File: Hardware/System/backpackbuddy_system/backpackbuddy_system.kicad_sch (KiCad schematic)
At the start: 1 part

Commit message: more changes
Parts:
- removed U?: ATmega32U4-A, Package_QFP:TQFP-44_10x10mm_P0.8mm, symbol MCU_Microchip_ATmega:ATmega32U4-A
- added J?: Ultrasonic 1, symbol Connector_Generic:Conn_01x04
- added J?: PIR, symbol Connector_Generic:Conn_01x03
- added J?: Ultrasonic 2, symbol Connector_Generic:Conn_01x04
- added J?: ESP8266, symbol Connector_Generic:Conn_01x08
- added SW?: RESET, symbol Switch:SW_Push
- added U?: ATmega32U4-A, Package_QFP:TQFP-44_10x10mm_P0.8mm, symbol MCU_Microchip_ATmega:ATmega32U4-A
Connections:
- net microcontroller/PB0: now also J?.3 (Pin_3)
- net microcontroller/PB1: now also J?.5 (Pin_5)
- net microcontroller/PB2: now also J?.2 (Pin_2)
- net microcontroller/PD0: now also J?.3 (Pin_3)
- net microcontroller/PD1: now also J?.2 (Pin_2)
- net microcontroller/PD4: now also J?.3 (Pin_3)
- net microcontroller/PD5: now also J?.2 (Pin_2)
- new net: J?.6 (Pin_6), SW?.1
- new net: U?.14 (VCC), U?.34 (VCC)
- new net: U?.15 (GND), U?.23 (GND), U?.35 (GND), U?.43 (GND)
- new net: U?.24 (AVCC), U?.44 (AVCC)
- new net +3V3: J?.4 (Pin_4), J?.8 (Pin_8)
- new net +5V: J?.3 (Pin_3), J?.4 (Pin_4), J?.4 (Pin_4)
- new net GND: J?.1 (Pin_1), J?.1 (Pin_1), J?.1 (Pin_1), J?.1 (Pin_1), SW?.2
- new net microcontroller/PD2/RX: J?.7 (Pin_7)
- new net microcontroller/PD3/TX: J?.2 (Pin_2)
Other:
- sheet microcontroller ports: added PD2/RX, PD3/TX; removed PB3, PB4, PB5, PB6, PB7, PC6, PC7, PD2, PD3

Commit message: vibration stuff
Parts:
- removed U?: ATmega32U4-A, Package_QFP:TQFP-44_10x10mm_P0.8mm, symbol MCU_Microchip_ATmega:ATmega32U4-A
- added J?: Left Vibration 2, symbol Connector_Generic:Conn_01x03
- added J?: Left Vibration 1, symbol Connector_Generic:Conn_01x03
- added J?: Right Vibration 2, symbol Connector_Generic:Conn_01x03
- added J?: Right Vibration 1, symbol Connector_Generic:Conn_01x03
- added Q? (x2): Q_NMOS_GDS, symbol Device:Q_NMOS_GDS
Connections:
- net +3V3: now also Q?.2 (D), Q?.2 (D)
- net GND: now also J?.1 (Pin_1), J?.1 (Pin_1), J?.1 (Pin_1), J?.1 (Pin_1), J?.3 (Pin_3), J?.3 (Pin_3), J?.3 (Pin_3), J?.3 (Pin_3)
- net microcontroller/PF5: now also Q?.1 (G)
- net microcontroller/PF6: now also Q?.1 (G)
- new net: J?.2 (Pin_2), J?.2 (Pin_2), Q?.3 (S) (x2)
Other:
- sheet microcontroller ports: added none; removed PD6, PD7, PE2, PE6, PF0, PF1, PF4, PF7
- moved on the sheet: J?, SW?

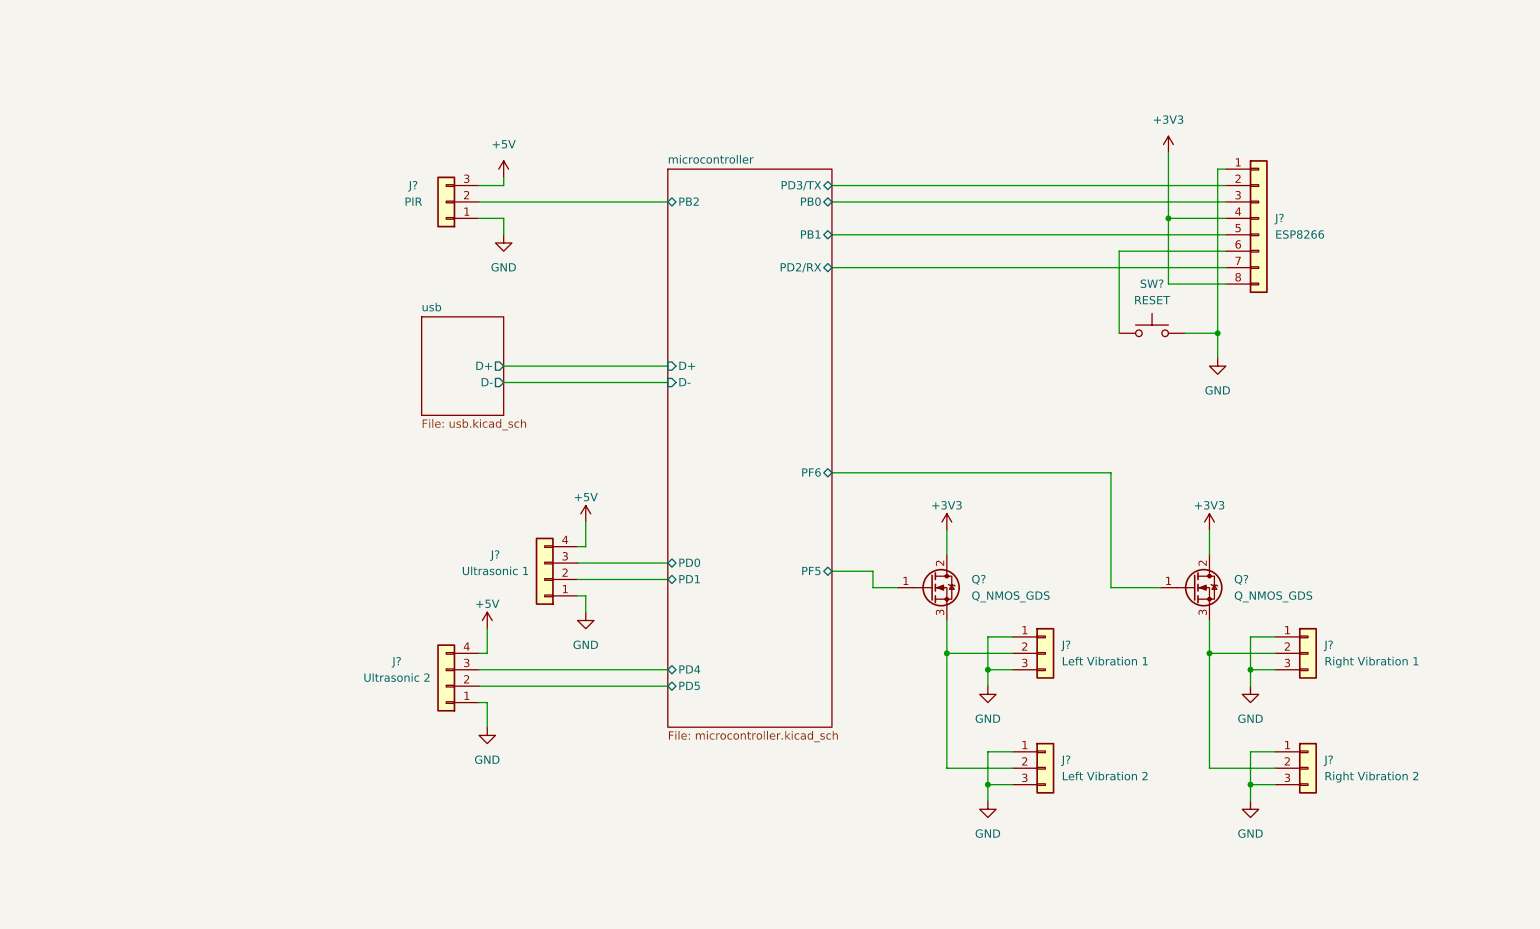
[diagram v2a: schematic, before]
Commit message: added safe connectors
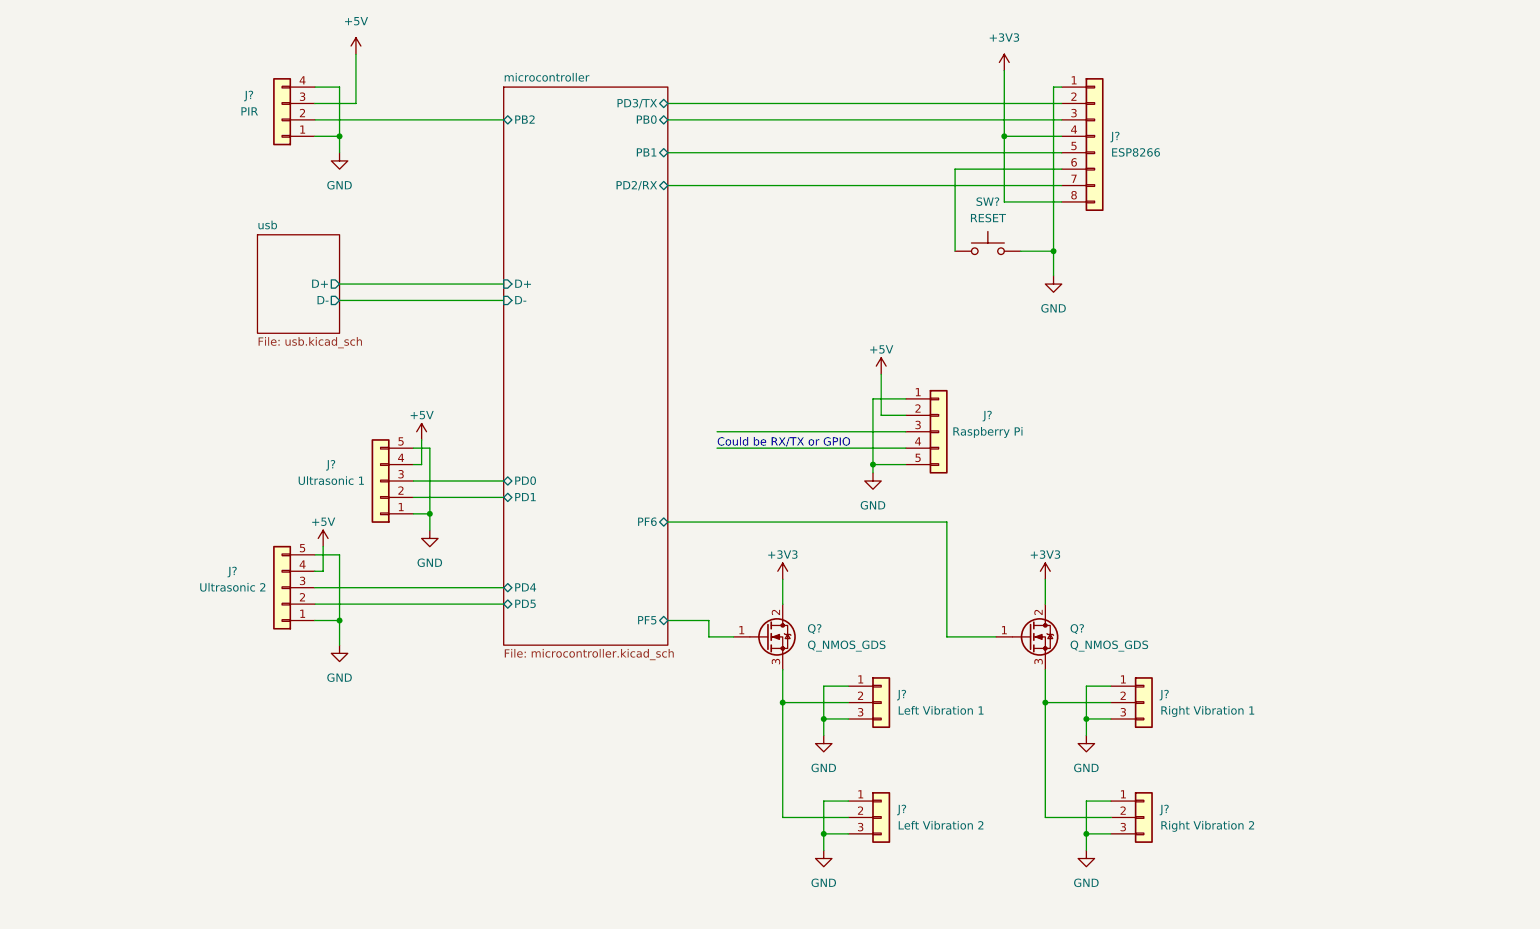
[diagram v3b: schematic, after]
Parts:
- removed J?: Ultrasonic 1, symbol Connector_Generic:Conn_01x04
- removed J?: PIR, symbol Connector_Generic:Conn_01x03
- removed J?: Ultrasonic 2, symbol Connector_Generic:Conn_01x04
- added J?: Ultrasonic 2, Connector_PinHeader_2.54mm:PinHeader_1x05_P2.54mm_Vertical, symbol Connector_Generic:Conn_01x05
- added J?: Ultrasonic 1, Connector_PinHeader_2.54mm:PinHeader_1x05_P2.54mm_Vertical, symbol Connector_Generic:Conn_01x05
- added J?: Raspberry Pi, Connector_PinHeader_2.54mm:PinHeader_1x05_P2.54mm_Vertical, symbol Connector_Generic:Conn_01x05
- added J?: PIR, symbol Connector_Generic:Conn_01x04
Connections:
- net +5V: now also J?.2 (Pin_2), J?.3 (Pin_3), J?.4 (Pin_4), J?.4 (Pin_4)
- net GND: now also J?.1 (Pin_1), J?.1 (Pin_1), J?.1 (Pin_1), J?.1 (Pin_1), J?.4 (Pin_4), J?.5 (Pin_5), J?.5 (Pin_5), J?.5 (Pin_5)
- net microcontroller/PB2: now also J?.2 (Pin_2)
- net microcontroller/PD0: now also J?.3 (Pin_3)
- net microcontroller/PD1: now also J?.2 (Pin_2)
- net microcontroller/PD4: now also J?.3 (Pin_3)
- net microcontroller/PD5: now also J?.2 (Pin_2)
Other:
- note added: "Could be RX/TX or GPIO"
- moved on the sheet: J?, Q?, SW?

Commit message: labels and stuff almost done
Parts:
- removed Q? (x2): Q_NMOS_GDS, symbol Device:Q_NMOS_GDS
- added Q? (x2): Q_NMOS_GSD, Package_TO_SOT_SMD:SOT-23_Handsoldering, symbol Device:Q_NMOS_GSD
- J? (x4): footprint (none) -> Connector_PinHeader_2.54mm:PinHeader_1x03_P2.54mm_Vertical; Stock (none) -> In connector kit
- J? (x3): Stock (none) -> In connector kit
- J?: footprint (none) -> Connector_PinHeader_2.54mm:PinHeader_2x04_P2.54mm_Vertical; Stock (none) -> In connector kit
- J?: footprint (none) -> Connector_PinHeader_2.54mm:PinHeader_1x04_P2.54mm_Vertical; Stock (none) -> In connector kit
- SW?: footprint (none) -> BackpackBuddyFootprintLibrary:RST_SW; MPN (none) -> HP0315AFKP2-R; Stock (none) -> https://www.digikey.com/en/products/detail/nkk-switches/HP0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
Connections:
- net +3V3: now also Q?.3 (D), Q?.3 (D)
- net microcontroller/PF5: now also Q?.1 (G)
- net microcontroller/PF6: now also Q?.1 (G)
- net at J?.2 (Pin_2), J?.2 (Pin_2): now also Q?.2 (S) (x2)

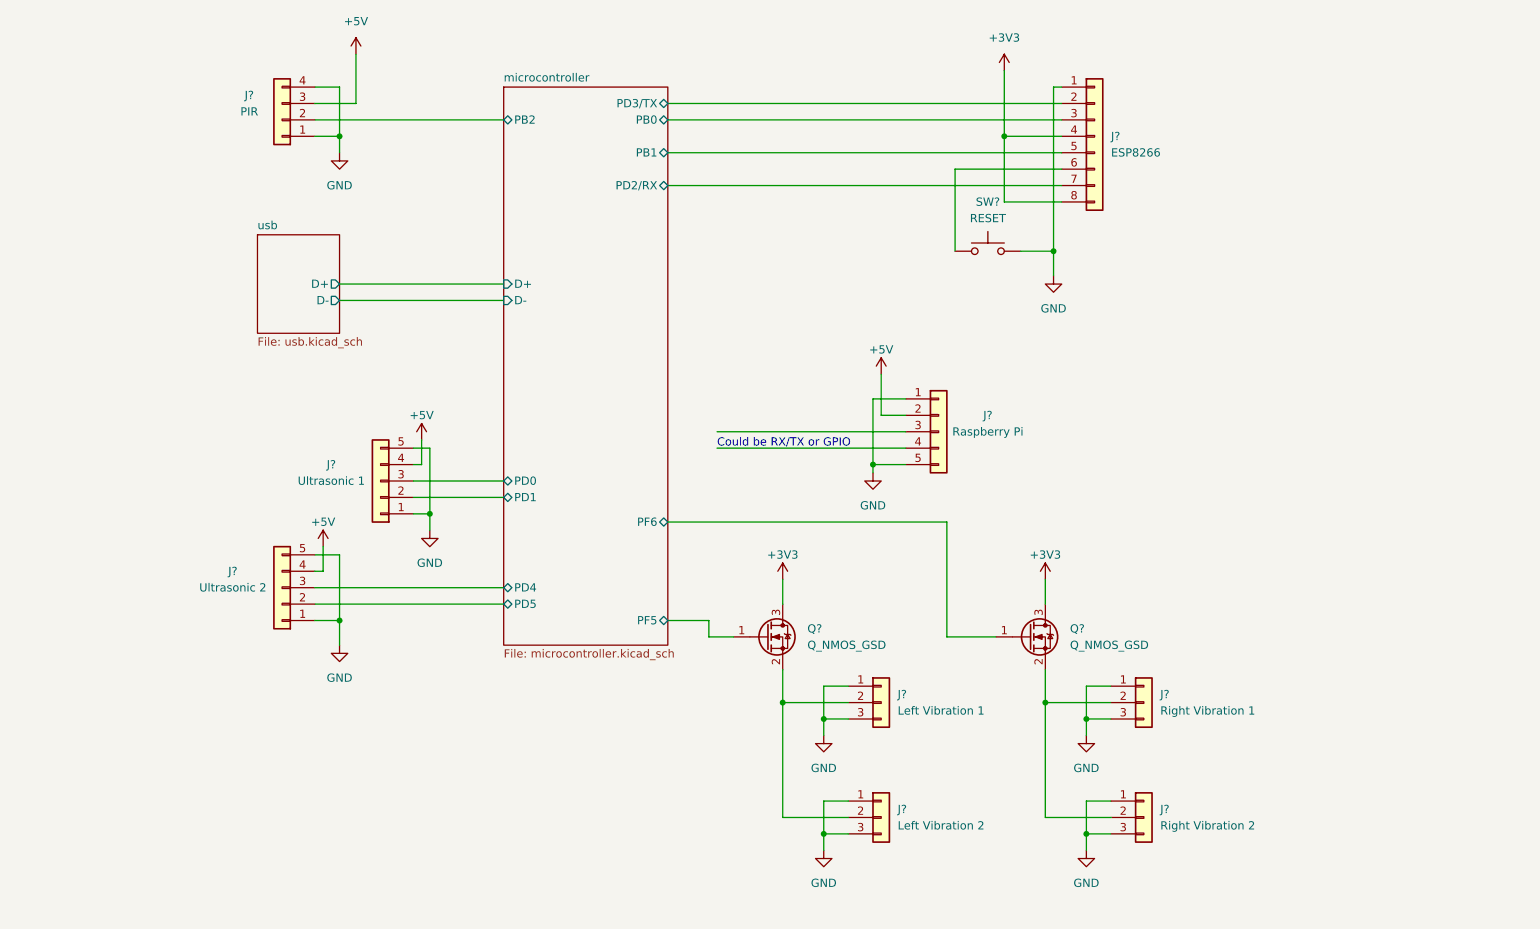
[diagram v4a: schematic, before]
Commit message: combining both sheets
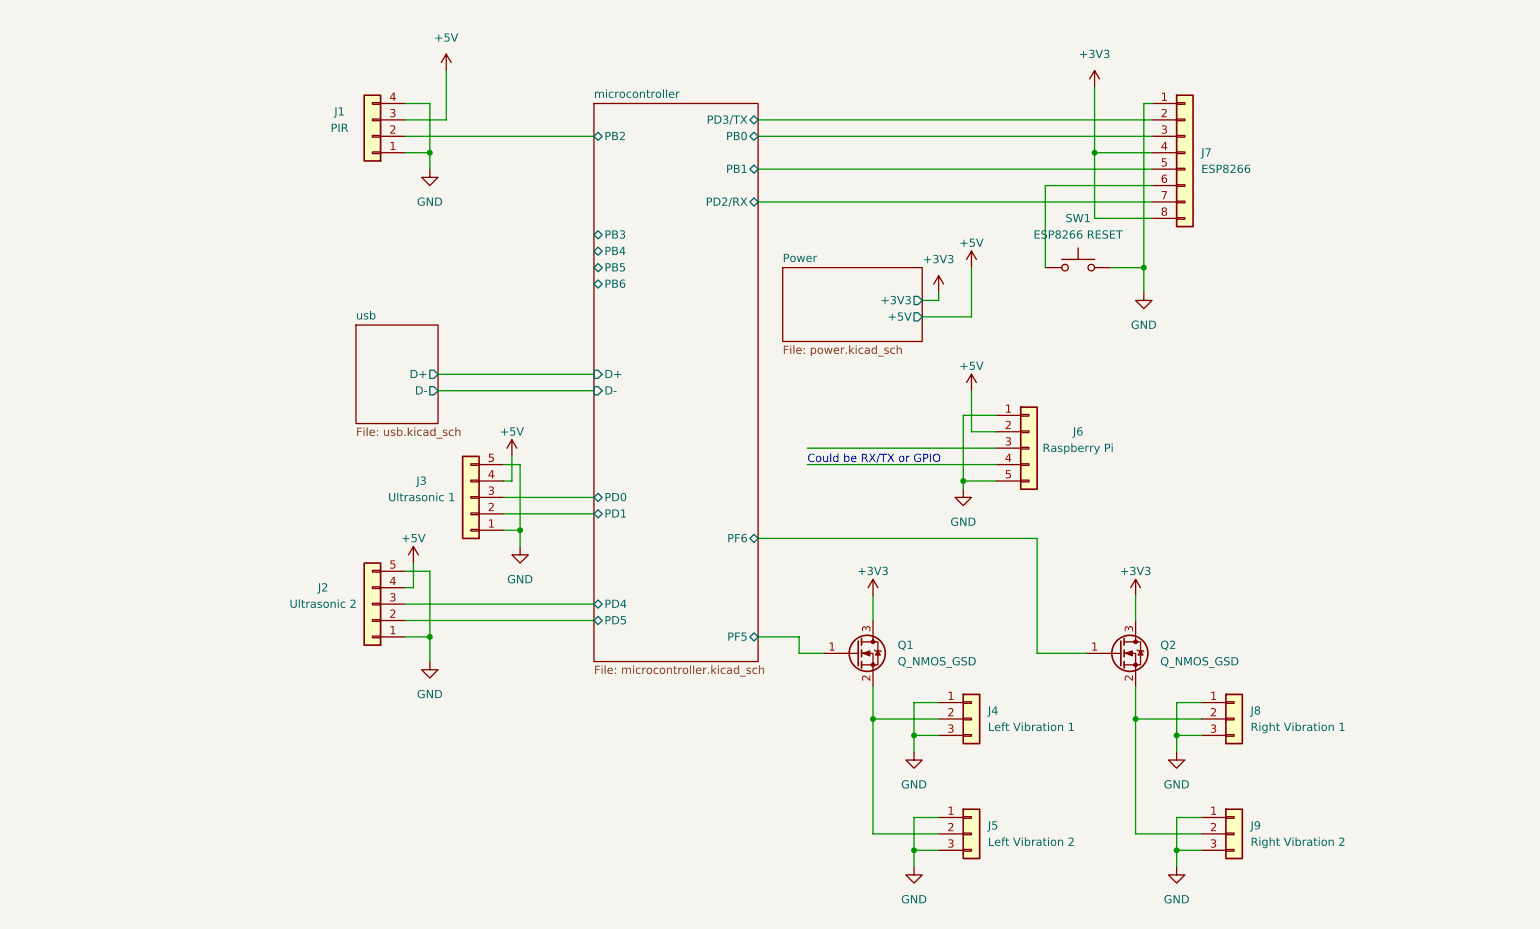
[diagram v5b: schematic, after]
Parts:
- SW1: renamed from SW?; value RESET -> ESP8266 RESET
- gave numbers to parts that had none: 11
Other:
- added sheet Power (power.kicad_sch)
- sheet microcontroller ports: added PB3, PB4, PB5, PB6; removed none
- moved on the sheet: J1, J2, J3, J4, J5, J6, J7, J8, J9, Q1, Q2, SW1

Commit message: more integration changes
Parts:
- added D10: Green, LED_SMD:LED_0603_1608Metric_Pad1.05x0.95mm_HandSolder, symbol Device:LED
- added D11: White, LED_SMD:LED_0603_1608Metric_Pad1.05x0.95mm_HandSolder, symbol Device:LED
- added D12: Yellow, LED_SMD:LED_0603_1608Metric_Pad1.05x0.95mm_HandSolder, symbol Device:LED
- added D9: Blue, LED_SMD:LED_0603_1608Metric_Pad1.05x0.95mm_HandSolder, symbol Device:LED
- added R10, R11, R12, R13: 1k, Resistor_SMD:R_0603_1608Metric_Pad1.05x0.95mm_HandSolder, symbol Device:R
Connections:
- net GND: now also D10.1 (K), D11.1 (K), D12.1 (K), D9.1 (K)
- net microcontroller/PB3: now also R10.1
- net microcontroller/PB4: now also R11.1
- net microcontroller/PB5: now also R12.1
- net microcontroller/PB6: now also R13.1
- new net: D10.2 (A), R11.2
- new net: D12.2 (A), R13.2
- new net: D11.2 (A), R12.2
- new net: D9.2 (A), R10.2

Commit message: updated fields
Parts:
- D10: MPN (none) -> LED GREEN CLEAR 0603 SMD; Stock (none) -> https://www.digikey.com/en/products/detail/w%C3%BCrth-elekt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
- D11: value White -> Yellow; MPN (none) -> LED YELLOW CLEAR 0603 SMD; Stock (none) -> https://www.digikey.com/en/products/detail/w%C3%BCrth-elekt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
- D12: value Yellow -> Amber; MPN (none) -> LED AMBER CLEAR 0603 SMD; Stock (none) -> https://www.digikey.com/en/products/detail/w%C3%BCrth-elekt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
- D9: MPN (none) -> LED BLUE CLEAR 0603 SMD; Stock (none) -> https://www.digikey.com/en/products/detail/w%C3%BCrth-elekt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
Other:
- note added: "Debug LEDs"
- moved on the sheet: D10, D11, D12, D9, J1, J2, J3, J4, J5, J6, J7, J8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

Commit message: schematic mostly done, just need to fix ERC, decoup caps, TP
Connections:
- net microcontroller/PD6: now reaches J6.3 (Pin_3)
- net microcontroller/PD7: now reaches J6.4 (Pin_4)
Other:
- sheet microcontroller ports: added PD6, PD7; removed none
- note removed: "Could be RX/TX or GPIO"
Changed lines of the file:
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@@
     (stroke (width 0) (type default) (color 0 0 0 0))
   )
-  (wire (pts (xy 165.1 93.98) (xy 194.31 93.98))
+  (wire (pts (xy 157.48 93.98) (xy 194.31 93.98))
     (stroke (width 0) (type default) (color 0 0 0 0))
   )
@@
     (stroke (width 0) (type default) (color 0 0 0 0))
   )
-  (wire (pts (xy 165.1 91.44) (xy 194.31 91.44))
+  (wire (pts (xy 157.48 91.44) (xy 194.31 91.44))
     (stroke (width 0) (type default) (color 0 0 0 0))
   )
@@
   (text "Debug LEDs" (at 48.26 111.76 0)
     (effects (font (size 3 3)) (justify left bottom))
-  )
-  (text "Could be RX/TX or GPIO\n" (at 165.1 93.98 0)
-    (effects (font (size 1.27 1.27)) (justify left bottom))
   )
   (symbol (lib_id "Device:LED") (at 55.88 91.44 90) (unit 1)
@@
       (effects (font (size 1.27 1.27)) (justify left))
     )
+    (pin "PD6" bidirectional (at 157.48 91.44 0)
+      (effects (font (size 1.27 1.27)) (justify right))
+    )
+    (pin "PD7" bidirectional (at 157.48 93.98 0)
+      (effects (font (size 1.27 1.27)) (justify right))
+    )
   )
   (sheet (at 95.25 72.39) (size 12.7 15.24) (fields_autoplaced)
@@
       (reference "#PWR025") (unit 1) (value "GND") (footprint "")
     )
-    (path "/cf3dbeef-e165-4b09-9181-2cdb640e2044/41aa3b43-a32d-49f1-9c0a-fe36fcc9cd50"
-      (reference "#PWR026") (unit 1) (value "GND") (footprint "")
-    )
     (path "/cf3dbeef-e165-4b09-9181-2cdb640e2044/983c869c-c01c-488c-ba8e-beda3e8d1dbf"
       (reference "#PWR027") (unit 1) (value "+5V") (footprint "")
@@
       (reference "#PWR0104") (unit 1) (value "GND") (footprint "")
     )
+    (path "/cf3dbeef-e165-4b09-9181-2cdb640e2044/6bf6a062-8950-4778-8e5f-ae7862f66350"
+      (reference "#PWR0105") (unit 1) (value "GND") (footprint "")
+    )
     (path "/af61f2eb-3376-4189-8310-620a433ef8ef/f4662e9e-a042-421d-9aa3-93a911a6004a"
       (reference "C1") (unit 1) (value "10pF") (footprint "Capacitor_SMD:C_0805_2012Metric_Pad1.18x1.45mm_HandSolder")
@@
     )
     (path "/af61f2eb-3376-4189-8310-620a433ef8ef/1d374c9e-2897-4c07-9d24-38daf6ec840d"
-      (reference "D1") (unit 1) (value "D") (footprint "")
+      (reference "D1") (unit 1) (value "50V") (footprint "Diode_SMD:D_SMB_Handsoldering")
     )
     (path "/31ba9691-809e-422e-95e0-c0a31dc5a8d2/61a90e4c-652d-4272-97e6-7c934e05c72d"
@@
       (reference "J9") (unit 1) (value "Right Vibration 2") (footprint "Connector_PinHeader_2.54mm:PinHeader_1x03_P2.54mm_Vertical")
     )
-    (path "/cf3dbeef-e165-4b09-9181-2cdb640e2044/3c9e1b60-734c-46b8-9d3d-6f93dd757851"
+    (path "/cf3dbeef-e165-4b09-9181-2cdb640e2044/db6c9d55-56d9-4594-900d-df9a65a357a3"
       (reference "J10") (unit 1) (value "USB_B_Micro") (footprint "Connector_USB:USB_Micro-B_Molex_47346-0001")
     )
@@
       (reference "J11") (unit 1) (value "Battery") (footprint "Connector_Molex:Molex_KK-254_AE-6410-03A_1x03_P2.54mm_Vertical")
     )
+    (path "/31ba9691-809e-422e-95e0-c0a31dc5a8d2/9ea34af7-405e-4360-b874-9b4cc86b0744"
+      (reference "JP1") (unit 1) (value "SolderJumper_2_Open") (footprint "Jumper:SolderJumper-2_P1.3mm_Open_RoundedPad1.0x1.5mm")
+    )
     (path "/31ba9691-809e-422e-95e0-c0a31dc5a8d2/25c24f9c-10e4-491d-ae1c-d8d731fa9c2b"
